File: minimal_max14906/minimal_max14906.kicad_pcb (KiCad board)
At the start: 4 copper layers, 34.3 x 21.6 mm, 56 parts, among them Q1 SI7309DN-T1-E3, Q2 SI7309DN-T1-E3, Q3 SI7309DN-T1-E3, Q4 SI7309DN-T1-E3, U1 MAX14906ATM+

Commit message: Minor updates
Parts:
- moved TP20 4.08 mm to (118.1, 116.8)
- moved TP21 4.08 mm to (119.4, 116.8)
- moved TP15 3.44 mm to (135.9, 116.8)
- moved TP16 3.44 mm to (134.6, 116.8)
- moved TP17 3.19 mm to (152.4, 116.8)
- moved TP24 3.19 mm to (151.1, 116.8)
- moved TP19 3.17 mm to (118.1, 90.2)
- moved TP22 3.17 mm to (119.4, 90.2)
- moved TP2 2.28 mm to (135.9, 90.2)
- moved TP7 2.28 mm to (129.5, 90.2)
- moved TP1 2.28 mm to (137.2, 90.2)
- moved TP10 2.28 mm to (141.0, 90.2)
- moved TP11 2.28 mm to (128.3, 90.2)
- moved TP12 2.28 mm to (127.0, 90.2)
- moved TP13 2.28 mm to (143.5, 90.2)
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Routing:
- net /D2_ISO: track 8.57 -> 11.1 mm
- net /D3_ISO: track 8.58 -> 11.1 mm
- net /D4_ISO: track 15.3 -> 17.8 mm
- net /D1_ISO: track 15.2 -> 17.8 mm
- net /MAX14906_EN_ISO: track 7.43 -> 9.97 mm
- net /MAX14906_SYNCH_ISO: track 6.81 -> 9.35 mm
- net /MAX14906_READY_ISO: track 8.10 -> 10.6 mm
- net /SPI1_SCK_ISO: track 5.82 -> 8.36 mm
- net /SPI1_MOSI_ISO: track 6.42 -> 8.96 mm
- net /SPI1_MISO_ISO: track 6.00 -> 8.54 mm
- net /SPI1_SS3_ISO: track 6.01 -> 8.55 mm
- net /MAX14906_FAULT_ISO: track 6.82 -> 9.36 mm
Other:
- board size 34.3 x 21.6 mm -> 39.4 x 26.7 mm

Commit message: Minor updates
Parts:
- added J1: CLP-102-02-G-D-BE, connector_footprints:CLP-102-02-G-D-BE, F.Cu at (116.2, 112.3)
- added J2: CLP-102-02-G-D-BE, connector_footprints:CLP-102-02-G-D-BE, F.Cu at (116.2, 94.5)
- added J3: CLP-102-02-G-D-BE, connector_footprints:CLP-102-02-G-D-BE, F.Cu at (154.3, 94.5)
- added J4: CLP-102-02-G-D-BE, connector_footprints:CLP-102-02-G-D-BE, F.Cu at (154.3, 112.3)
- added J5: CLP-114-02-G-D-BE, connector_footprints:CLP-114-02-G-D-BE, F.Cu at (135.3, 88.2)
- added J6: CLP-104-02-G-D-BE, connector_footprints:CLP-104-02-G-D-BE, F.Cu at (154.3, 103.4)
- added J7: CLP-104-02-G-D-BE, connector_footprints:CLP-104-02-G-D-BE, F.Cu at (116.2, 103.4)
- added TP25: TestPoint, test_point_footprints:TestPoint_THTPad_Castelated, F.Cu at (111.8, 99.6)
- added TP26: TestPoint, test_point_footprints:TestPoint_THTPad_Castelated, F.Cu at (111.8, 107.2)
- moved TP15 28.6 mm to (158.7, 99.6), turned to 180 degrees
- moved TP16 26.0 mm to (158.7, 107.2), turned to 180 degrees
- moved TP1 10.2 mm to (137.2, 79.9)
- moved TP10 10.2 mm to (141.0, 79.9)
- moved TP11 10.2 mm to (128.3, 79.9)
- moved TP12 10.2 mm to (127.0, 79.9)
- moved TP13 10.2 mm to (143.5, 79.9)
- moved TP14 10.2 mm to (142.2, 79.9)
- moved TP2 10.2 mm to (135.9, 79.9)
- moved TP3 10.2 mm to (134.6, 79.9)
- moved TP4 10.2 mm to (133.4, 79.9)
- moved TP5 10.2 mm to (132.1, 79.9)
- moved TP6 10.2 mm to (130.8, 79.9)
- moved TP7 10.2 mm to (129.5, 79.9)
- moved TP8 10.2 mm to (138.4, 79.9)
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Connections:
- net /3V3_ISO renamed /3V3
- net /D1_ISO renamed /D1
- net /D2_ISO renamed /D2
- net /D3_ISO renamed /D3
- net /D4_ISO renamed /D4
- net /MAX14906_EN_ISO renamed /EN
- net /MAX14906_FAULT_ISO renamed /~{FAULT}
- net /MAX14906_READY_ISO renamed /~{READY}
- net /MAX14906_SYNCH_ISO renamed /SYNCH
- net /SPI1_MISO_ISO renamed /SDO
- net /SPI1_MOSI_ISO renamed /SDI
- net /SPI1_SCK_ISO renamed /CLK
- net /SPI1_SS3_ISO renamed /~{CS}
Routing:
- net /~{CS}: track 8.55 -> 19.2 mm
- net /CLK: track 8.36 -> 19.0 mm
- net /SDO: track 8.54 -> 19.1 mm
- net /SDI: track 8.96 -> 19.4 mm
- net /D1: track 17.8 -> 28.1 mm, vias 1 -> 2
- net /D4: track 17.8 -> 28.1 mm, vias 1 -> 2
- net /SYNCH: track 9.35 -> 19.6 mm
- net /D2: track 11.1 -> 21.3 mm, vias 1 -> 2
- net /D3: track 11.1 -> 21.3 mm, vias 1 -> 2
- net /3V3: track 13.0 -> 23.2 mm, vias 2 -> 4
- net /~{FAULT}: track 9.36 -> 19.5 mm
- net /EN: track 9.97 -> 19.6 mm
- net /~{READY}: track 10.6 -> 19.9 mm
- net /FLED: track 21.8 -> 28.9 mm
- net /SLED: track 20.6 -> 21.2 mm
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- added copper zone on In1.Cu, net /CHANNEL_1
- added copper zone on In1.Cu, net /CHANNEL_2
- added copper zone on In1.Cu, net /CHANNEL_3
- added copper zone on In1.Cu, net /CHANNEL_4
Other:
- board size 39.4 x 26.7 mm -> 47 x 36.8 mm

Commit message: Update subproject commit for KiCAD Symbol Generator
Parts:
- renumbered C5 to C1, C12 to C10, C7 to C11, C6 to C12, C9 to C13, C8 to C2, C2 to C3, C13 to C4, C4 to C5, C11 to C6, C3 to C7, C10 to C8, C1 to C9, D9 to D1, D8 to D2, D4 to D3, D7 to D4, D3 to D5, D2 to D7, D5 to D8, D1 to D9, J5 to J1, J7 to J4, J6 to J5, J1 to J6, J4 to J7, Q2 to Q1, Q4 to Q2, Q1 to Q3, Q3 to Q4, R5 to R1, R4 to R2, R2 to R4, R1 to R5, TP12 to TP1, TP8 to TP10, TP9 to TP11, TP10 to TP12, TP14 to TP13, TP13 to TP14, TP22 to TP15, TP23 to TP16, TP19 to TP17, TP25 to TP19, TP11 to TP2, TP15 to TP20, TP26 to TP21, TP16 to TP22, TP20 to TP23, TP17 to TP24, TP21 to TP25, TP24 to TP26, TP7 to TP3, TP6 to TP4, TP4 to TP6, TP3 to TP7, TP2 to TP8, TP1 to TP9

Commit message: Minor updates to project files
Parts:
- moved TP1 10.2 mm to (127.0, 90.1)
- moved TP10 10.2 mm to (138.4, 90.1)
- moved TP11 10.2 mm to (139.7, 90.1)
- moved TP12 10.2 mm to (141.0, 90.1)
- moved TP13 10.2 mm to (142.2, 90.1)
- moved TP14 10.2 mm to (143.5, 90.1)
- moved TP2 10.2 mm to (128.3, 90.1)
- moved TP3 10.2 mm to (129.5, 90.1)
- moved TP4 10.2 mm to (130.8, 90.1)
- moved TP5 10.2 mm to (132.1, 90.1)
- moved TP6 10.2 mm to (133.4, 90.1)
- moved TP7 10.2 mm to (134.6, 90.1)
- moved TP8 10.2 mm to (135.9, 90.1)
- moved TP9 10.2 mm to (137.2, 90.1)
- moved J1 2.54 mm to (135.3, 85.6)
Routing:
- net /D4: track 28.1 -> 24.2 mm
- net /D1: track 28.1 -> 24.2 mm
- net /SDO: track 19.1 -> 15.3 mm
- net /SYNCH: track 19.6 -> 15.7 mm
- net /~{CS}: track 19.2 -> 15.3 mm
- net /~{FAULT}: track 19.5 -> 15.6 mm
- net /SDI: track 19.4 -> 15.5 mm
- net /CLK: track 19.0 -> 15.1 mm
- net /EN: track 19.6 -> 15.7 mm
- net /D2: track 21.3 -> 17.5 mm
- net /D3: track 21.3 -> 17.5 mm
- net /3V3: track 23.2 -> 19.6 mm
- net /~{READY}: track 19.9 -> 18.1 mm
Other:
- board size 47 x 36.8 mm -> 47 x 34.9 mm

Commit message: Minor updates to project files
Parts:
- moved TP20 7.24 mm to (153.0, 104.1)
- moved TP19 7.24 mm to (117.5, 104.1)
- moved TP16 6.11 mm to (153.0, 94.1)
- moved TP18 6.02 mm to (153.0, 95.2)
- moved TP22 6.02 mm to (153.0, 105.3)
- moved TP24 6.02 mm to (153.0, 111.7)
- moved TP26 6.02 mm to (153.0, 113.0)
- moved TP15 6.02 mm to (117.5, 93.9)
- moved TP17 6.02 mm to (117.5, 95.2)
- moved TP21 6.02 mm to (117.5, 105.3)
- moved TP23 6.02 mm to (117.5, 111.7)
- moved TP25 6.02 mm to (117.5, 113.0)
- moved J2 3.17 mm to (113.0, 94.5)
- moved J4 3.17 mm to (113.0, 103.4)
- moved J6 3.17 mm to (113.0, 112.3)
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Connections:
- J1 pad 1: /D3 -> GNDA
- J1 pad 11: /CLK -> GNDA
- J1 pad 13: /SDO -> GNDA
- J1 pad 17: /3V3 -> GNDA
- J1 pad 19: /~{FAULT} -> GNDA
- J1 pad 21: /EN -> GNDA
- J1 pad 23: /~{READY} -> GNDA
- J1 pad 25: /D1 -> GNDA
- J1 pad 27: /D2 -> GNDA
- J1 pad 3: /D4 -> GNDA
- J1 pad 5: /SYNCH -> GNDA
- J1 pad 7: /SDI -> GNDA
- J1 pad 9: /~{CS} -> GNDA
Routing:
- net /3V3: track 19.6 -> 14.3 mm, vias 4 -> 3
- net /~{READY}: track 18.1 -> 13.8 mm
- net /~{CS}: track 15.3 -> 11.2 mm
- net /SYNCH: track 15.7 -> 11.6 mm
- net /SDI: track 15.5 -> 11.4 mm
- net /CLK: track 15.1 -> 11.0 mm
- net /SDO: track 15.3 -> 11.2 mm
- net /D1: track 24.2 -> 20.1 mm, vias 2 -> 1
- net /D2: track 17.5 -> 13.4 mm, vias 2 -> 1
- net /D3: track 17.5 -> 13.4 mm, vias 2 -> 1
- net /EN: track 15.7 -> 11.6 mm
- net /~{FAULT}: track 15.6 -> 11.5 mm
- net /D4: track 24.2 -> 20.1 mm, vias 2 -> 1
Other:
- board size 47 x 34.9 mm -> 52.1 x 34.9 mm

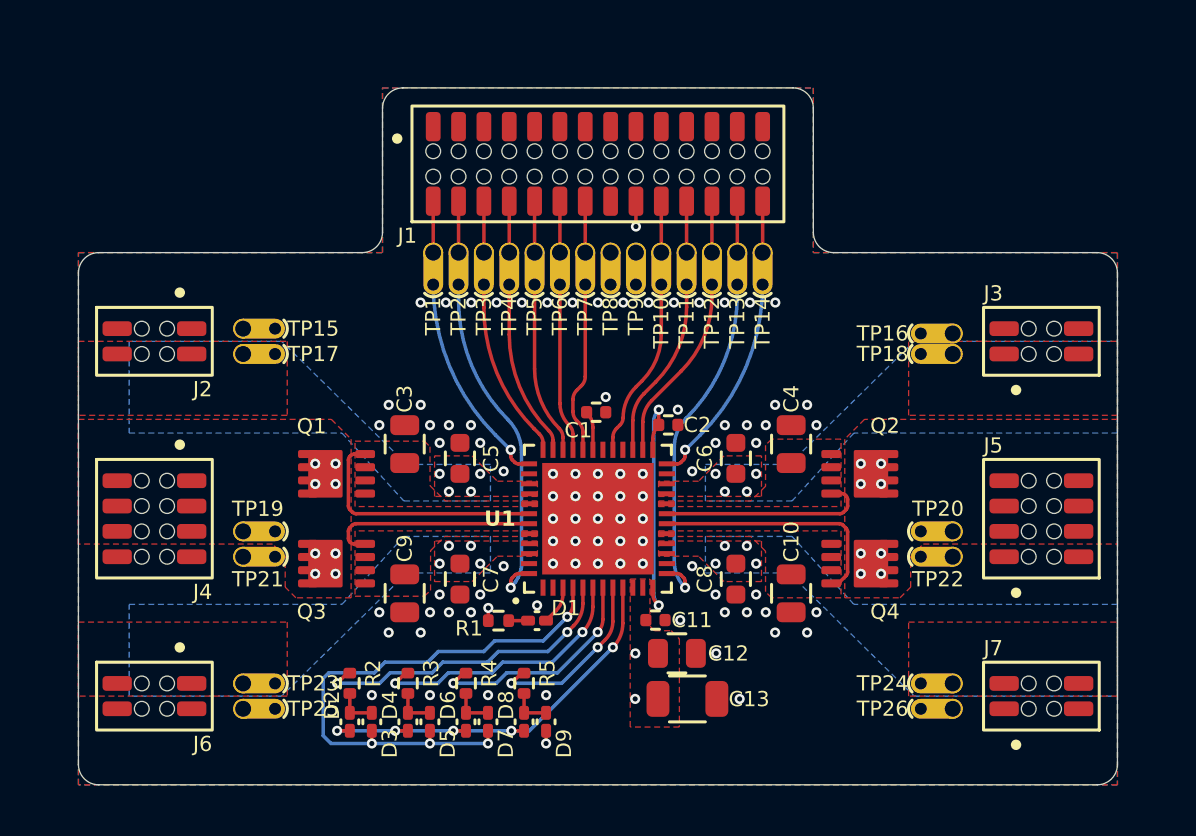
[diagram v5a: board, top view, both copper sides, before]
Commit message: Update KiCAD Symbol Generator subproject commit and adjust pad dimensions
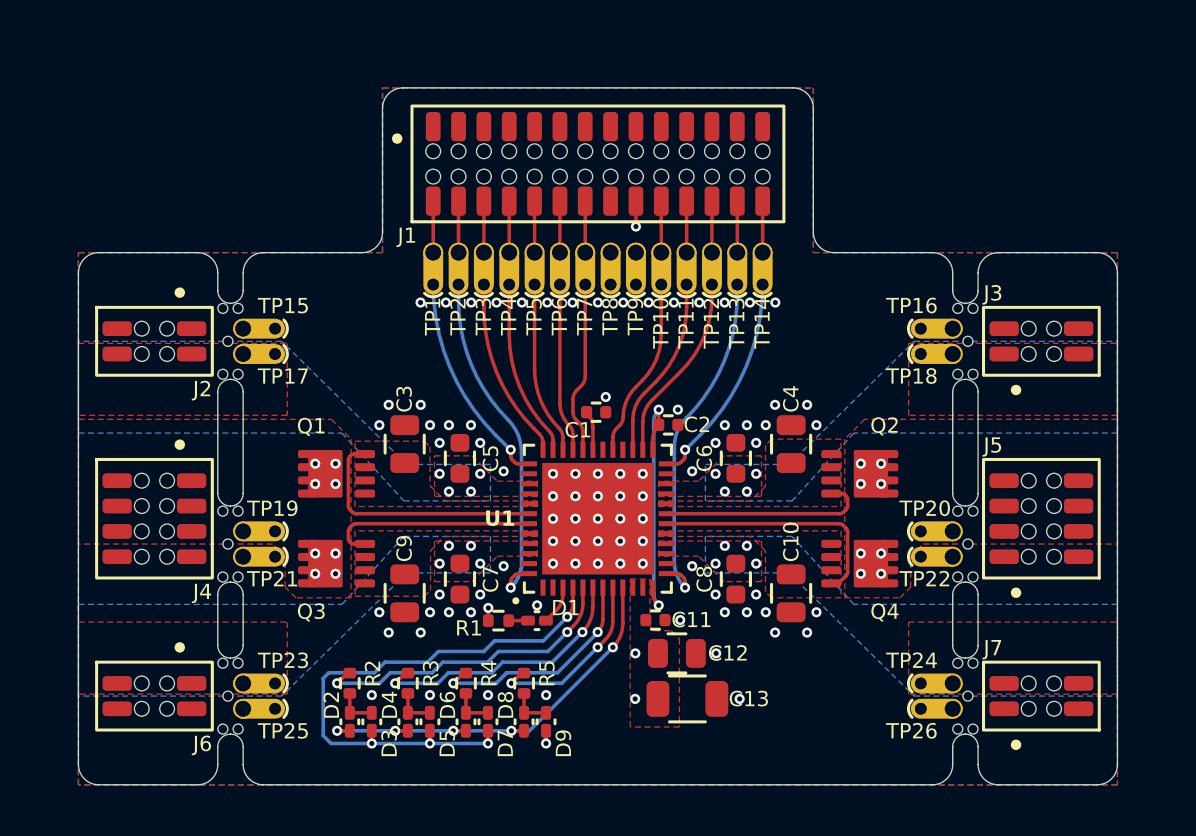
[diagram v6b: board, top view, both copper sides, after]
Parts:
- added REF**: mouse-bite-midle-50mil-200mil, mouse_bite_footprints:mouse-bite-midle-50mil-200mil, F.Cu at (116.8, 112.3)
- added REF**: mouse-bite-midle-50mil-200mil, mouse_bite_footprints:mouse-bite-midle-50mil-200mil, F.Cu at (153.7, 104.7)
- added REF**: mouse-bite-midle-50mil-200mil, mouse_bite_footprints:mouse-bite-midle-50mil-200mil, F.Cu at (116.8, 104.7)
- added REF**: mouse-bite-midle-50mil-200mil, mouse_bite_footprints:mouse-bite-midle-50mil-200mil, F.Cu at (153.7, 112.3)
- added REF**: mouse-bite-midle-50mil-200mil, mouse_bite_footprints:mouse-bite-midle-50mil-200mil, F.Cu at (116.8, 94.5)
- added REF**: mouse-bite-midle-50mil-200mil, mouse_bite_footprints:mouse-bite-midle-50mil-200mil, F.Cu at (153.7, 94.5)
- moved TP16 0.24 mm to (153.0, 93.9)
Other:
- outline, holes or cut-outs redrawn

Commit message: Backup
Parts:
- added REF**: mouse-bite-50mil-790mil, mouse_bite_footprints:mouse-bite-50mil-790mil, F.Cu at (135.3, 89.6)
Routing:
- net /FLED: track 28.9 -> 31.8 mm
- net /3V3: track 14.3 -> 13.0 mm, vias 3 -> 2
- added copper zone on F.Cu, net /3V3
- added copper zone on In1.Cu, net GNDA
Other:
- outline, holes or cut-outs redrawn

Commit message: Minor updates
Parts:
- moved J3 1.27 mm to (158.7, 94.5)
- moved J5 1.27 mm to (158.7, 103.4)
- moved J7 1.27 mm to (158.7, 112.3)
- moved J2 1.27 mm to (111.8, 94.5)
- moved J4 1.27 mm to (111.8, 103.4)
- moved J6 1.27 mm to (111.8, 112.3)
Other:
- board size 52.1 x 34.9 mm -> 55.9 x 34.9 mm
